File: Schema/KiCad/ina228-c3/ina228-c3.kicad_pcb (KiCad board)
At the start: 2 copper layers, 104.8 x 37 mm, 51 parts, among them J1 Terminal, U1 XL7015E1, U2 HT7833, U3 INA238, U4 ESP32-C3-WROOM-02, U5 CP2102N-Axx-xQFN28, U6 CA-IS3741HW, U7 USBLC6-2P6

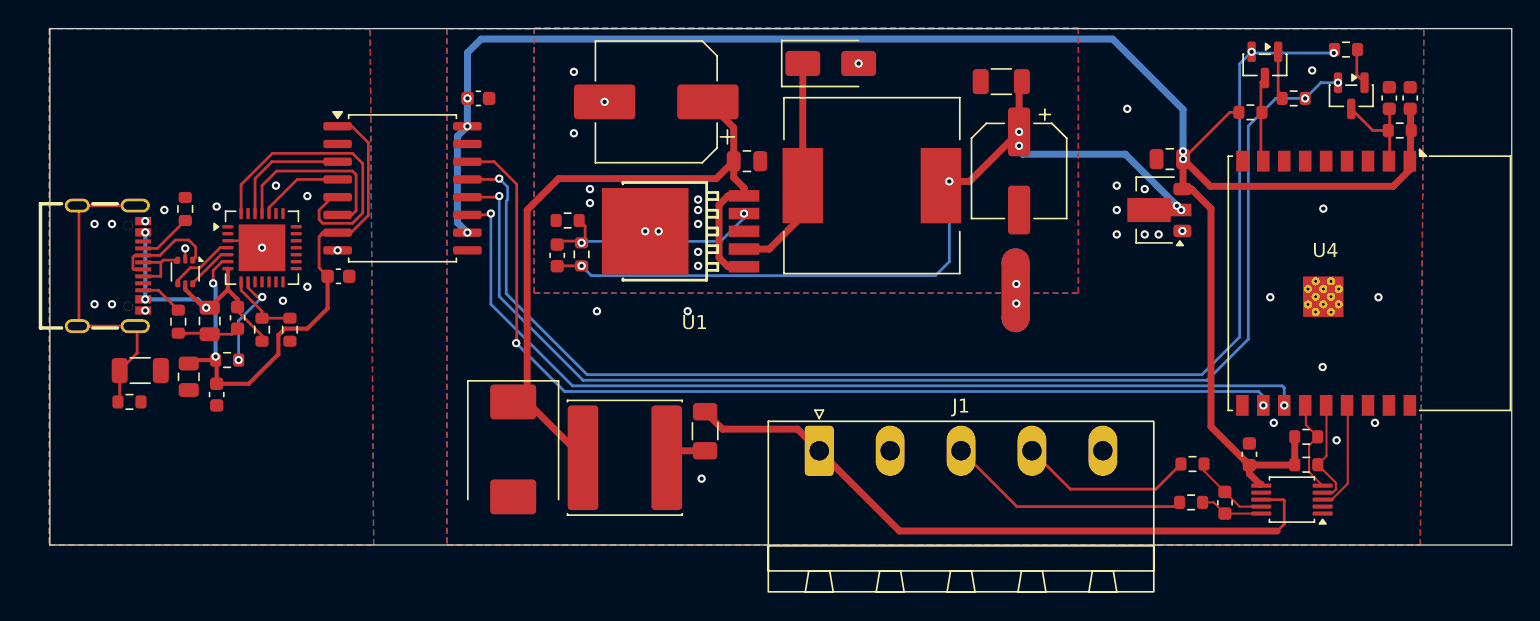
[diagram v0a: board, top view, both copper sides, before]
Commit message: Remove usb2uart chip, making the design simpler (but probably more expensive.)
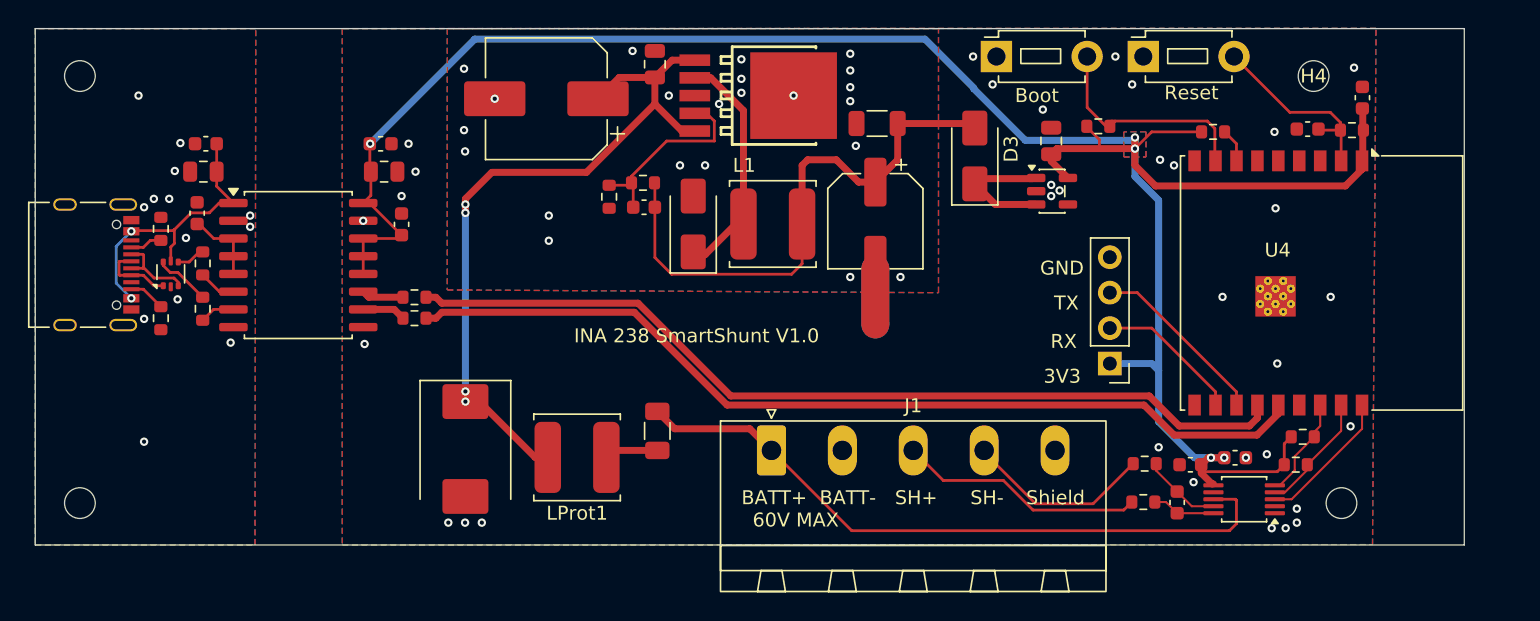
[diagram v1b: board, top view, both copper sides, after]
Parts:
- removed C8: 10nF 500V, Capacitor_SMD:C_1206_3216Metric
- removed CVDD1: 100nF 16V, Capacitor_SMD:C_0603_1608Metric
- removed CVDD2: 4.7nF, Capacitor_SMD:C_0805_2012Metric
- removed QEN1, QPROG1: BC847, Package_TO_SOT_SMD:SOT-23
- removed R3: 22K, Resistor_SMD:R_0603_1608Metric
- removed R4: 47K, Resistor_SMD:R_0603_1608Metric
- removed RBEN1, RBPRG1: 10K, Resistor_SMD:R_0603_1608Metric
- removed RPU3: 1K, Resistor_SMD:R_0603_1608Metric
- removed RSH1: 1M, Resistor_SMD:R_0603_1608Metric
- removed U5: CP2102N-Axx-xQFN28, Package_DFN_QFN:QFN-28-1EP_5x5mm_P0.5mm_EP3.35x3.35mm
- added CF3: 4.7nF 16V, Capacitor_SMD:C_0603_1608Metric, F.Cu at (155.0, 84.2)
- added CVUSB3: 100nF 16V, Capacitor_SMD:C_0603_1608Metric, F.Cu at (80.6, 66.7)
- added CVUSB4: 4.7nF, Capacitor_SMD:C_0805_2012Metric, F.Cu at (94.0, 63.8)
- added D3: SS14, Diode_SMD:D_SMA, F.Cu at (136.3, 62.6)
- added H1: MountingHole, MountingHole:MountingHole_2.2mm_M2_DIN965, F.Cu at (72.2, 56.9)
- added H2: MountingHole, MountingHole:MountingHole_2.2mm_M2_DIN965, F.Cu at (72.2, 87.5)
- added H3: MountingHole, MountingHole:MountingHole_2.2mm_M2_DIN965, F.Cu at (162.6, 87.5)
- added H4: MountingHole, MountingHole:MountingHole_2.2mm_M2_DIN965, F.Cu at (160.6, 56.9)
- added J2: UART-Conn, Connector_PinHeader_2.54mm:PinHeader_1x04_P2.54mm_Vertical, F.Cu at (146.0, 77.5)
- added RD1: 24R, Resistor_SMD:R_0603_1608Metric, F.Cu at (81.0, 70.3)
- added RD2: 24R, Resistor_SMD:R_0603_1608Metric, F.Cu at (96.2, 74.2)
- added RD3: 24R, Resistor_SMD:R_0603_1608Metric, F.Cu at (96.2, 72.8)
- added RD4: 24R, Resistor_SMD:R_0603_1608Metric, F.Cu at (81.0, 73.6)
- added RPUPG2: 10K, Resistor_SMD:R_0603_1608Metric, F.Cu at (153.4, 60.9)
- added SW1: Reset, Button_Switch_THT:SW_PUSH_1P1T_6x3.5mm_H4.3_APEM_MJTP1243, F.Cu at (148.4, 55.5)
- added SW2: Boot, Button_Switch_THT:SW_PUSH_1P1T_6x3.5mm_H4.3_APEM_MJTP1243, F.Cu at (137.9, 55.5)
- C6: value 10uF 10V -> 22uF
- JUSB1: footprint easyeda:USB-C-SMD_TYPE-C16PIN -> Connector_USB:USB_C_Receptacle_Palconn_UTC16-G
- L1: value 100uH (1,2A) -> 100uH 1A; footprint Inductor_SMD:L_12x12mm_H6mm -> Inductor_SMD:L_TDK_VLS6045EX_VLS6045AF
- LProt1: value 47uH, >1,5A -> 100uH 1A; footprint Inductor_SMD:L_Sunlord_SWPA8040S -> Inductor_SMD:L_TDK_VLS6045EX_VLS6045AF
- R1: value 30K -> 33K
- U2: value HT7833 -> AP2112K-3.3; footprint Package_TO_SOT_SMD:SOT-89-3 -> Package_TO_SOT_SMD:SOT-23-5
- U6: value CA-IS3741HW -> ADUM3160
- moved D2 15.1 mm to (116.2, 67.5), turned to 90 degrees
- moved CVUSB2 12.7 mm to (81.2, 61.8), turned to 0 degrees
- moved RPUPG1 10.9 mm to (145.2, 60.5)
- moved C4 10.9 mm to (129.2, 67.3)
- moved CVUSB1 10.7 mm to (81.0, 63.8), turned to 0 degrees
- moved U1 10.4 mm to (119.8, 58.3), turned to 0 degrees
- moved NT1 10.1 mm to (129.2, 72.7)
- moved NT2 10.1 mm to (129.2, 72.7)
- moved C2 9.58 mm to (113.4, 56.0), turned to -90 degrees
- moved C3 9.39 mm to (129.3, 60.3)
- moved U6 9.28 mm to (87.8, 70.4)
- moved C6 8.60 mm to (141.8, 61.5), turned to 90 degrees
- moved C1 7.88 mm to (105.6, 58.5)
- moved CVDD4 7.72 mm to (93.8, 61.8)
- moved L1 7.61 mm to (121.8, 67.5)
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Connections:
- CVDD3 pad 1: Net-(U5-VDD) -> +3V3
- CVDD3 pad 2: USB-GND -> GND1
- CVUSB1 pad 2: Net-(U5-VREGIN) -> Net-(U6-VBUS1)
- CVUSB2 pad 2: Net-(U5-VREGIN) -> Net-(U6-VBUS1)
- U2 pad 1: GND1 -> Net-(D3-K)
- U2 pad 2: +5V -> GND1
- U2 pad 3: +3V3 -> Net-(D3-K)
- U4 pad 11: UART-RX -> RXD
- U4 pad 12: UART-TX -> TXD
- U4 pad 13: I2C-SCL -> DD-
- U4 pad 14: I2C-SDA -> DD+
- U4 pad 15: INA-AL -> unconnected-(U4-IO3-Pad15)
- U4 pad 16: unconnected-(U4-IO2-Pad16) -> I2C-SCL
- U4 pad 17: unconnected-(U4-IO1-Pad17) -> I2C-SDA
- U4 pad 18: unconnected-(U4-IO0-Pad18) -> INA-AL
- U4 pad 7: unconnected-(U4-IO8-Pad7) -> Net-(U4-IO8)
- U6 pad 1: Net-(U5-VDD) -> Net-(U6-VBUS1)
- U6 pad 10: +3V3 -> Net-(U6-DD+)
- U6 pad 11: UART-TX -> Net-(U6-DD-)
- U6 pad 12: DTR -> +3V3
- U6 pad 13: RTS -> +3V3
- U6 pad 14: UART-RX -> +3V3
- U6 pad 2: unconnected-(U6-GNDA-Pad2) -> USB-GND
- U6 pad 3: Net-(U5-TXD) -> Net-(U6-PDEN)
- U6 pad 4: Net-(U5-~{RTS}) -> Net-(U6-PDEN)
- U6 pad 5: Net-(U5-~{DTR}) -> Net-(U6-PDEN)
- U6 pad 7: Net-(U5-VDD) -> Net-(U6-UD+)
- U7 pad 1: Net-(JUSB1-D--PadA7) -> Net-(JUSB1-D+-PadA6)
- U7 pad 3: Net-(JUSB1-D+-PadA6) -> Net-(JUSB1-D--PadA7)
- U7 pad 5: Net-(U5-VREGIN) -> Net-(U6-VBUS1)
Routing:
- net RTS: track 93.6 -> 0.00 mm, vias 3 -> 0
- net DTR: track 89.9 -> 0.00 mm, vias 3 -> 0
- net UART-RX: track 71.4 -> 0.00 mm, vias 2 -> 0
- net UART-TX: track 68.8 -> 0.00 mm, vias 2 -> 0
- net DD+: track 0.00 -> 66.2 mm
- net DD-: track 0.00 -> 64.6 mm
- net Net-(U5-VDD): track 40.3 -> 0.00 mm, vias 2 -> 0
- net +3V3: track 131.6 -> 157.1 mm
- net Net-(JUSB1-SHIELD): track 23.0 -> 0.00 mm
- net Net-(U5-~{DTR}): track 21.5 -> 0.00 mm
- net Net-(U6-VBUS1): track 0.00 -> 21.1 mm, vias 0 -> 2
- net Net-(U5-VREGIN): track 19.8 -> 0.00 mm, vias 3 -> 0
- net +5V: track 59.6 -> 40.4 mm, vias 6 -> 0
- net TXD: track 0.00 -> 13.0 mm
- net Net-(U6-UD-): track 13.3 -> 2.70 mm
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- added copper zone on B.Cu, net +3V3
- added copper zone on F.Cu, net +3V3
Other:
- board size 104.8 x 37 mm -> 102.4 x 37 mm
- board text added: "3V3"
- board text added: "60V MAX"
- board text added: "BATT+"
- board text added: "BATT-"
- board text added: "GND"
- board text added: "INA 238 SmartShunt V1.0"
- board text added: "RX"
- board text added: "SH+"
- board text added: "SH-"
- board text added: "Shield"
- board text added: "TX"
